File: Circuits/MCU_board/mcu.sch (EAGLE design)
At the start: 40 parts, among them IC1 RP111N331B-TR-FE, U1 TCA9548APWR, U2 USBLC6-2P6, U3 LD39050PU33R, U4 LSM9DS1, U5 STM32L452RECT6

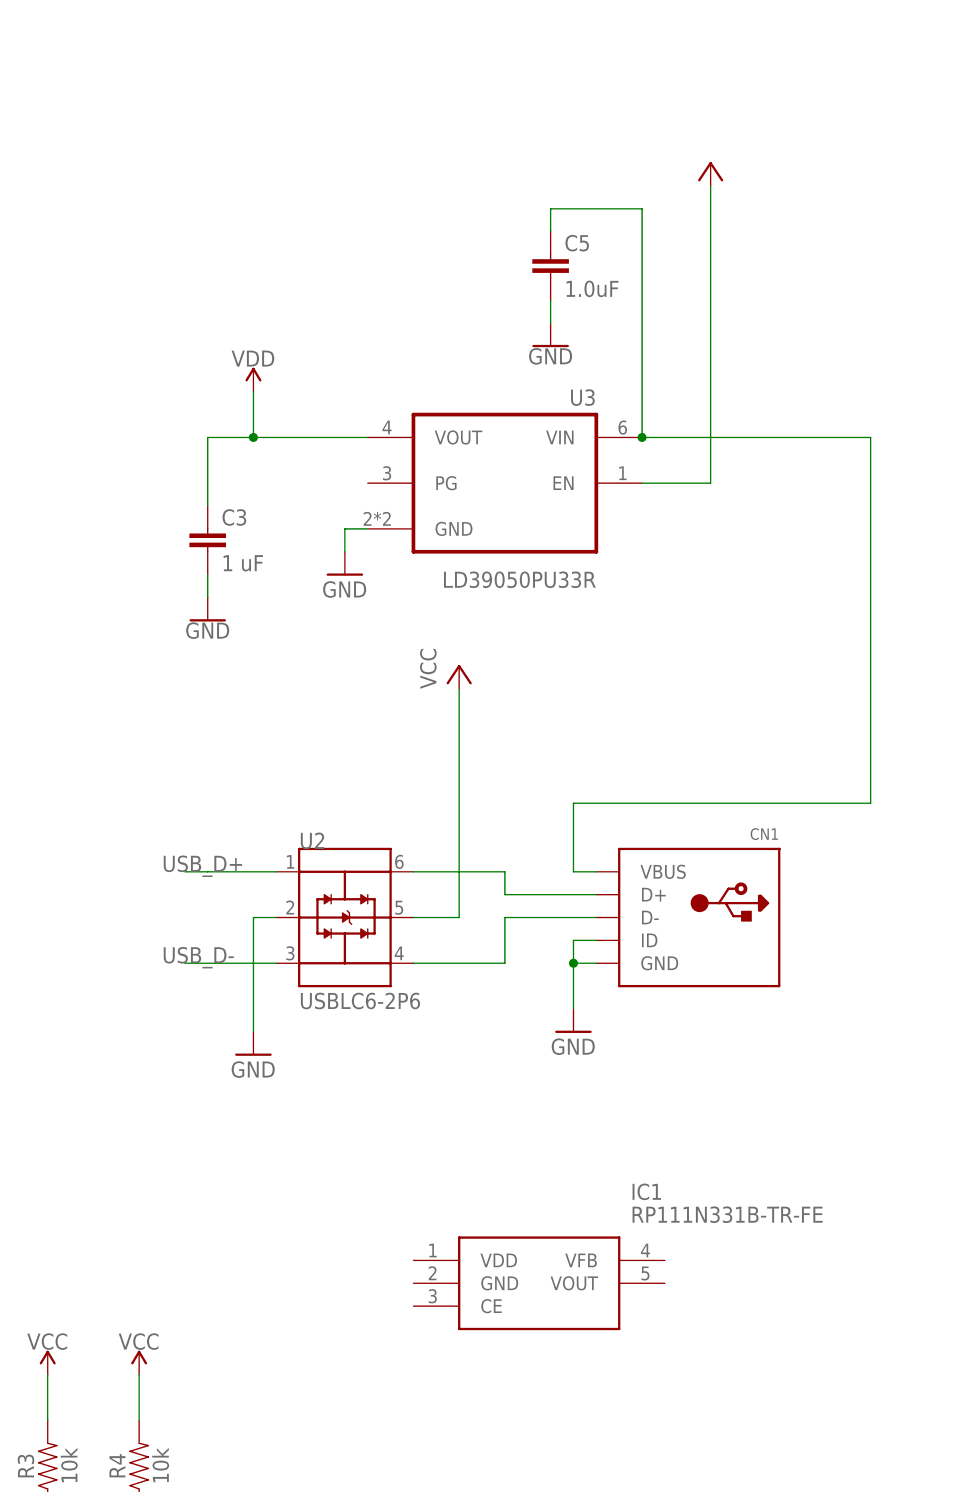
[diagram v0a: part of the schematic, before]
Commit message: Added LDO and fixed TVS diode connection
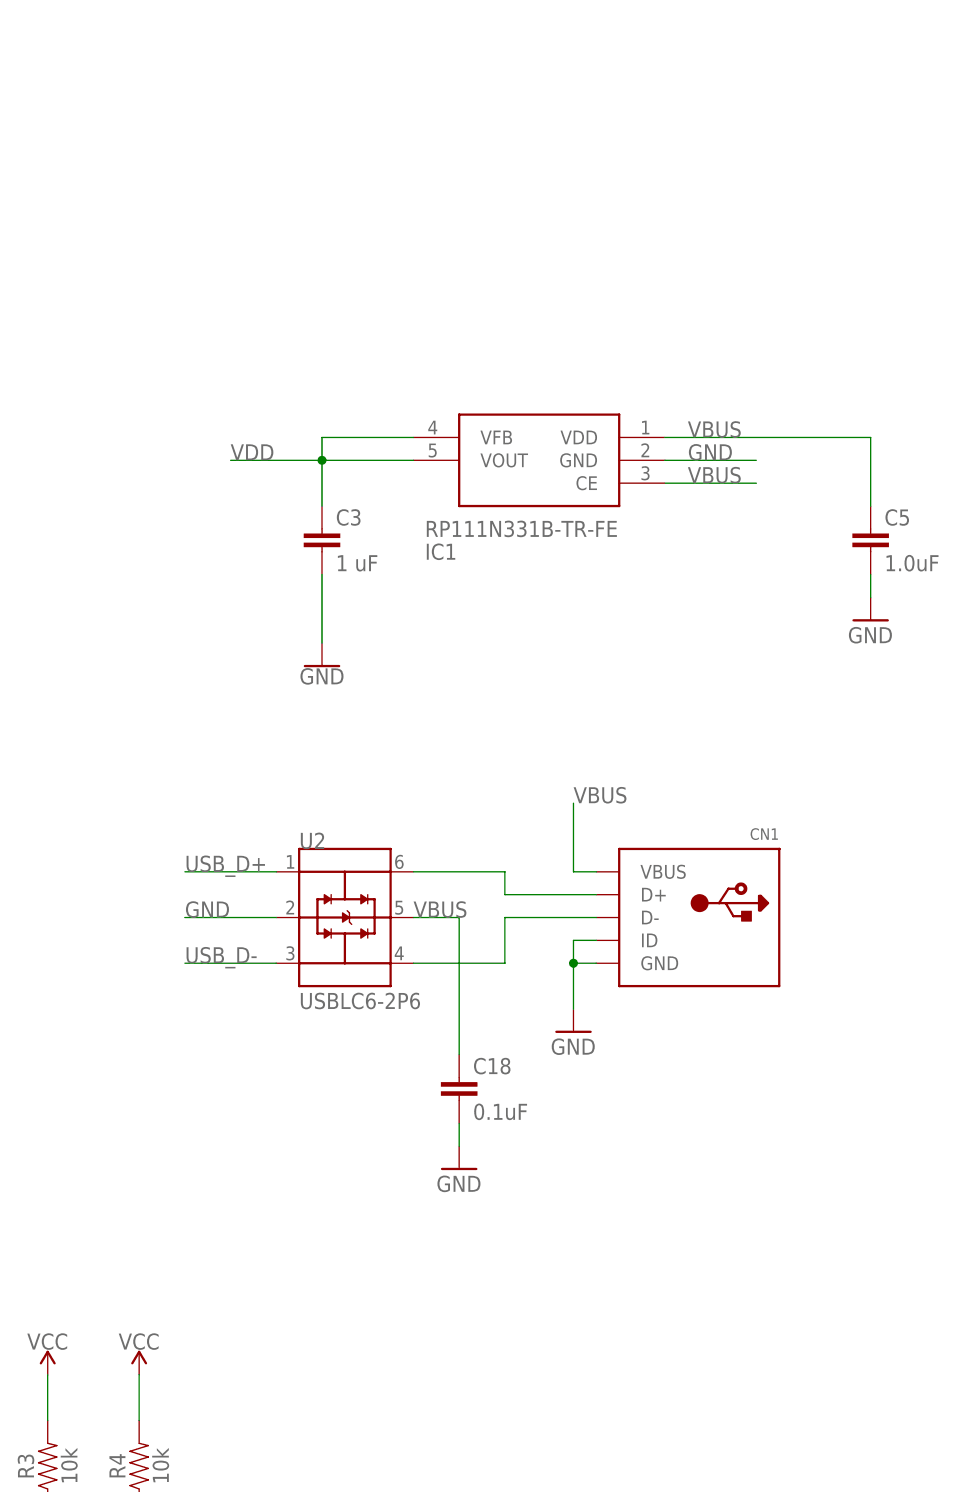
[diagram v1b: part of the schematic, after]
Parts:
- removed U3: LD39050PU33R, LD39050PU33R:LD39050PU33R
- added C18: 0.1uF, SparkFun-Capacitors:0.1UF-0603-25V-(+80/-20%)
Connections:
- removed net N$3: C5.1, CN1.VBUS, U3.VIN
- new net VBUS: C18.1, C5.1, CN1.VBUS, IC1.CE, IC1.VDD, U2.VBUS
- net GND: now also C18.2, IC1.GND; no longer U3.GND
- net VCC: no longer U2.VBUS, U3.EN
- net VDD: now also IC1.VFB, IC1.VOUT; no longer U3.VOUT
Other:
- moved on the sheet: C3, C5, IC1

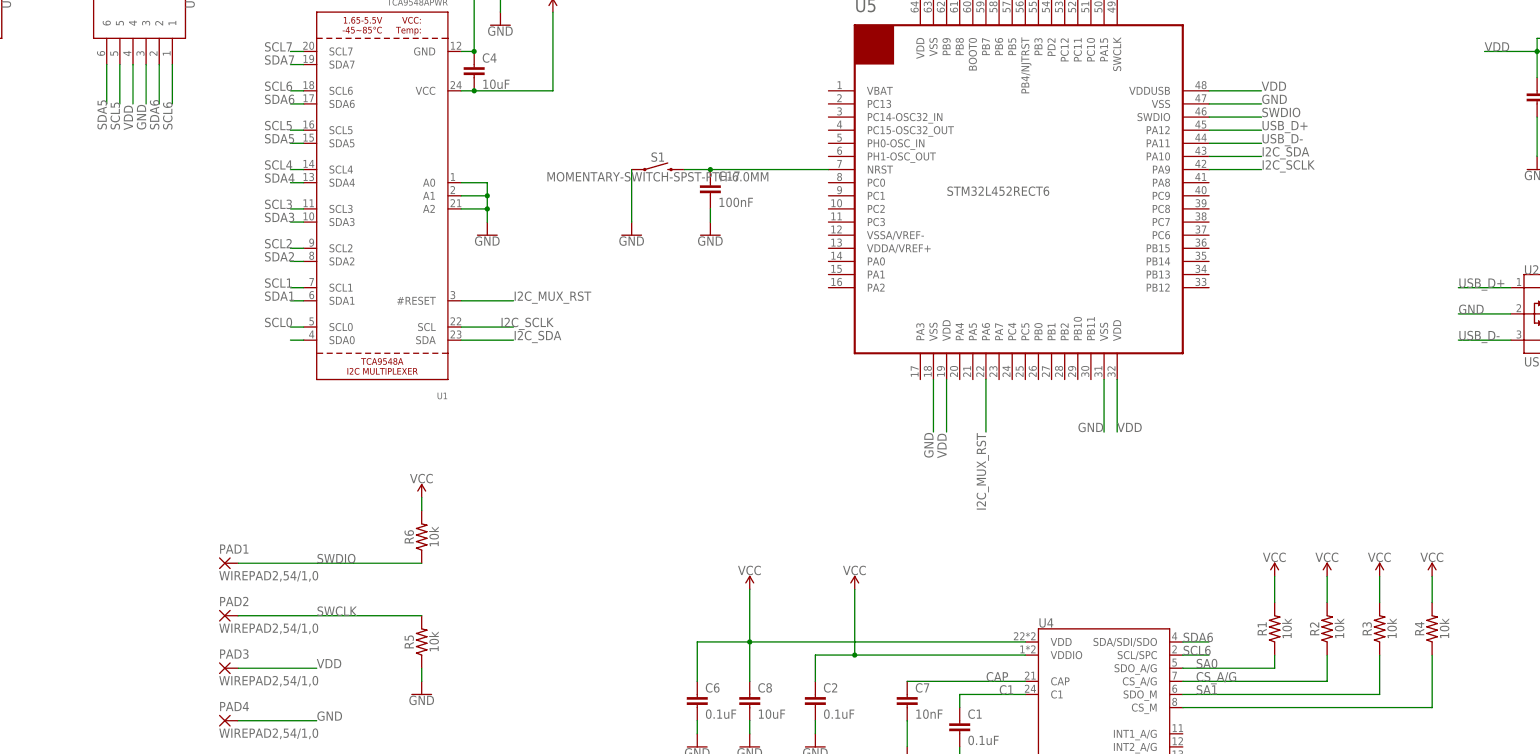
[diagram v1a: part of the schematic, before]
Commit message: Changed all VCC to VDD, Fixed i2c bus issue for board IMU and baseboard IMU
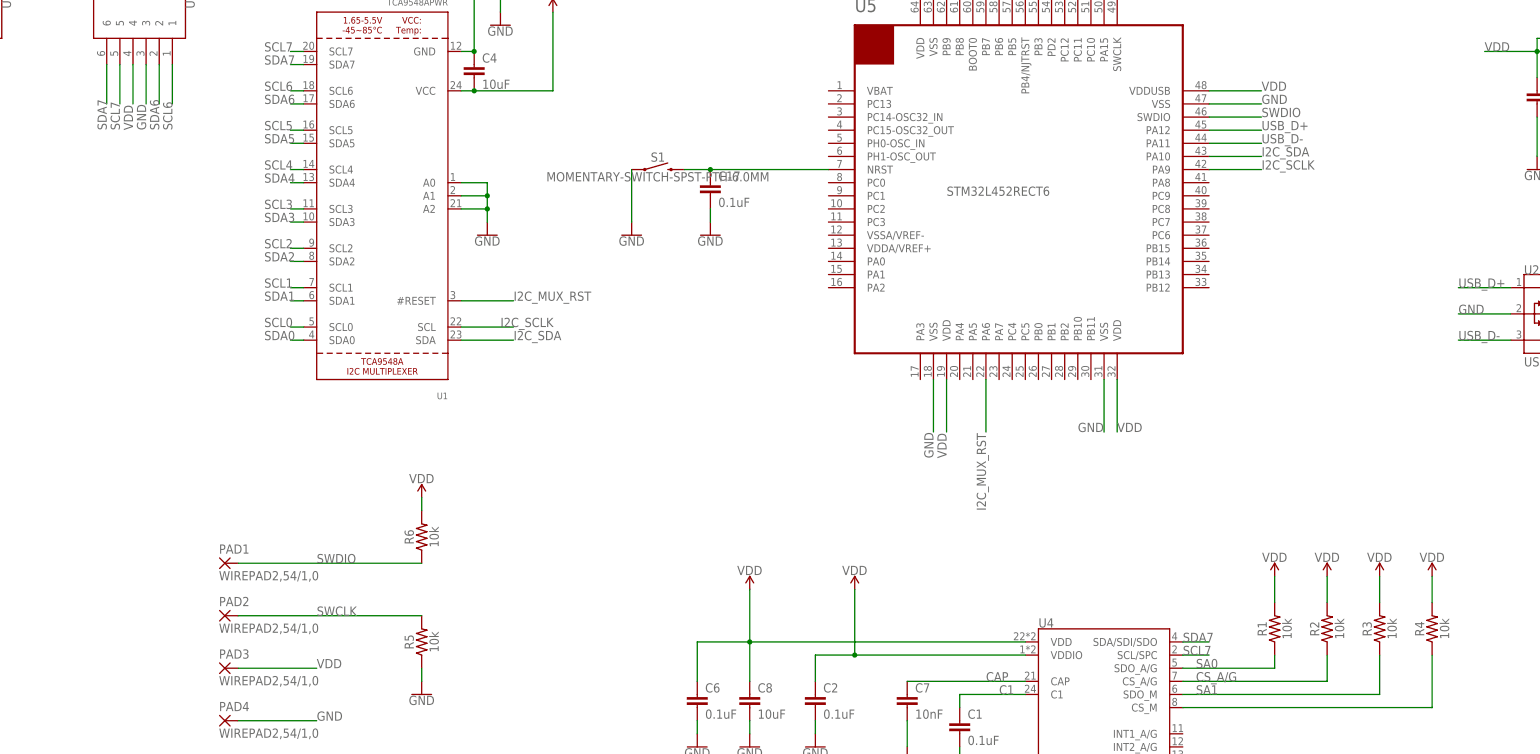
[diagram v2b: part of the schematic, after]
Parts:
- C17: value 100nF -> 0.1uF; device SparkFun-Capacitors:0.18UF-0603-10V-10% -> SparkFun-Capacitors:0.1UF-0603-25V-(+80/-20%)
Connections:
- removed net VCC: C2.1, C6.1, C8.1, R1.2, R2.2, R3.2, R4.2, R6.2, U4.VDD, U4.VDDIO
- net SCL5: no longer U$5.5
- net SCL6: no longer U4.SCL/SPC
- net SCL7: now also U$5.5, U4.SCL/SPC
- net SDA5: no longer U$5.6
- net SDA6: no longer U4.SDA/SDI/SDO
- net SDA7: now also U$5.6, U4.SDA/SDI/SDO
- net VDD: now also C2.1, C6.1, C8.1, R1.2, R2.2, R3.2, R4.2, R6.2, U4.VDD, U4.VDDIO

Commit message: Added i2c resistors - pulled high, Fixed capacitor package size, moved schematics around to be more organized
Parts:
- added R10, R11, R12, R13, R14, R15, R16, R17, R18, R19, R20, R7, R8, R9: 4.7k, SparkFun-Resistors:4.7KOHM-0603-1/10W-1%
- C10, C12, C14, C16: device SparkFun-Capacitors:0.18UF-0603-10V-10% -> SparkFun-Capacitors:4.7UF-0603-6.3V-(10%)
- C11, C13, C15, C9: value 100nF -> 0.1uF; device SparkFun-Capacitors:0.18UF-0603-10V-10% -> SparkFun-Capacitors:0.1UF-0603-25V-(+80/-20%)
- C3: value 1 uF -> 1.0uF; device SparkFun-Capacitors:0.18UF-0603-10V-10% -> SparkFun-Capacitors:1.0UF-0603-16V-10%-X7R
- C5: device SparkFun-Capacitors:1.0UF-0402-16V-10% -> SparkFun-Capacitors:1.0UF-0603-16V-10%-X7R
- R1, R3: value 10k -> 4.7k; device SparkFun-Resistors:10KOHM-0603-1/10W-1% -> SparkFun-Resistors:4.7KOHM-0603-1/10W-1%
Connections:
- removed net SA0: R1.1, U4.SDO_A/G
- removed net SA1: R3.1, U4.SDO_M
- new net N$3: C17.1
- net GND: now also U4.SDO_A/G, U4.SDO_M
- net N$4: no longer C17.1
- net SCL0: now also R3.1
- net SCL1: now also R8.1
- net SCL2: now also R10.1
- net SCL3: now also R12.1
- net SCL4: now also R14.1
- net SCL5: now also R16.1
- net SCL6: now also R18.1
- net SCL7: now also R20.1
- net SDA0: now also R1.1
- net SDA1: now also R7.1
- net SDA2: now also R9.1
- net SDA3: now also R11.1
- net SDA4: now also R13.1
- net SDA5: now also R15.1
- net SDA6: now also R17.1
- net SDA7: now also R19.1
- net VDD: now also R10.2, R11.2, R12.2, R13.2, R14.2, R15.2, R16.2, R17.2, R18.2, R19.2, R20.2, R7.2, R8.2, R9.2
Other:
- moved on the sheet: C1, C10, C11, C12, C13, C14, C15, C16, C17, C18, C2, C3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
